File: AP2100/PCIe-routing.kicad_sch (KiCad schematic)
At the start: 40 parts

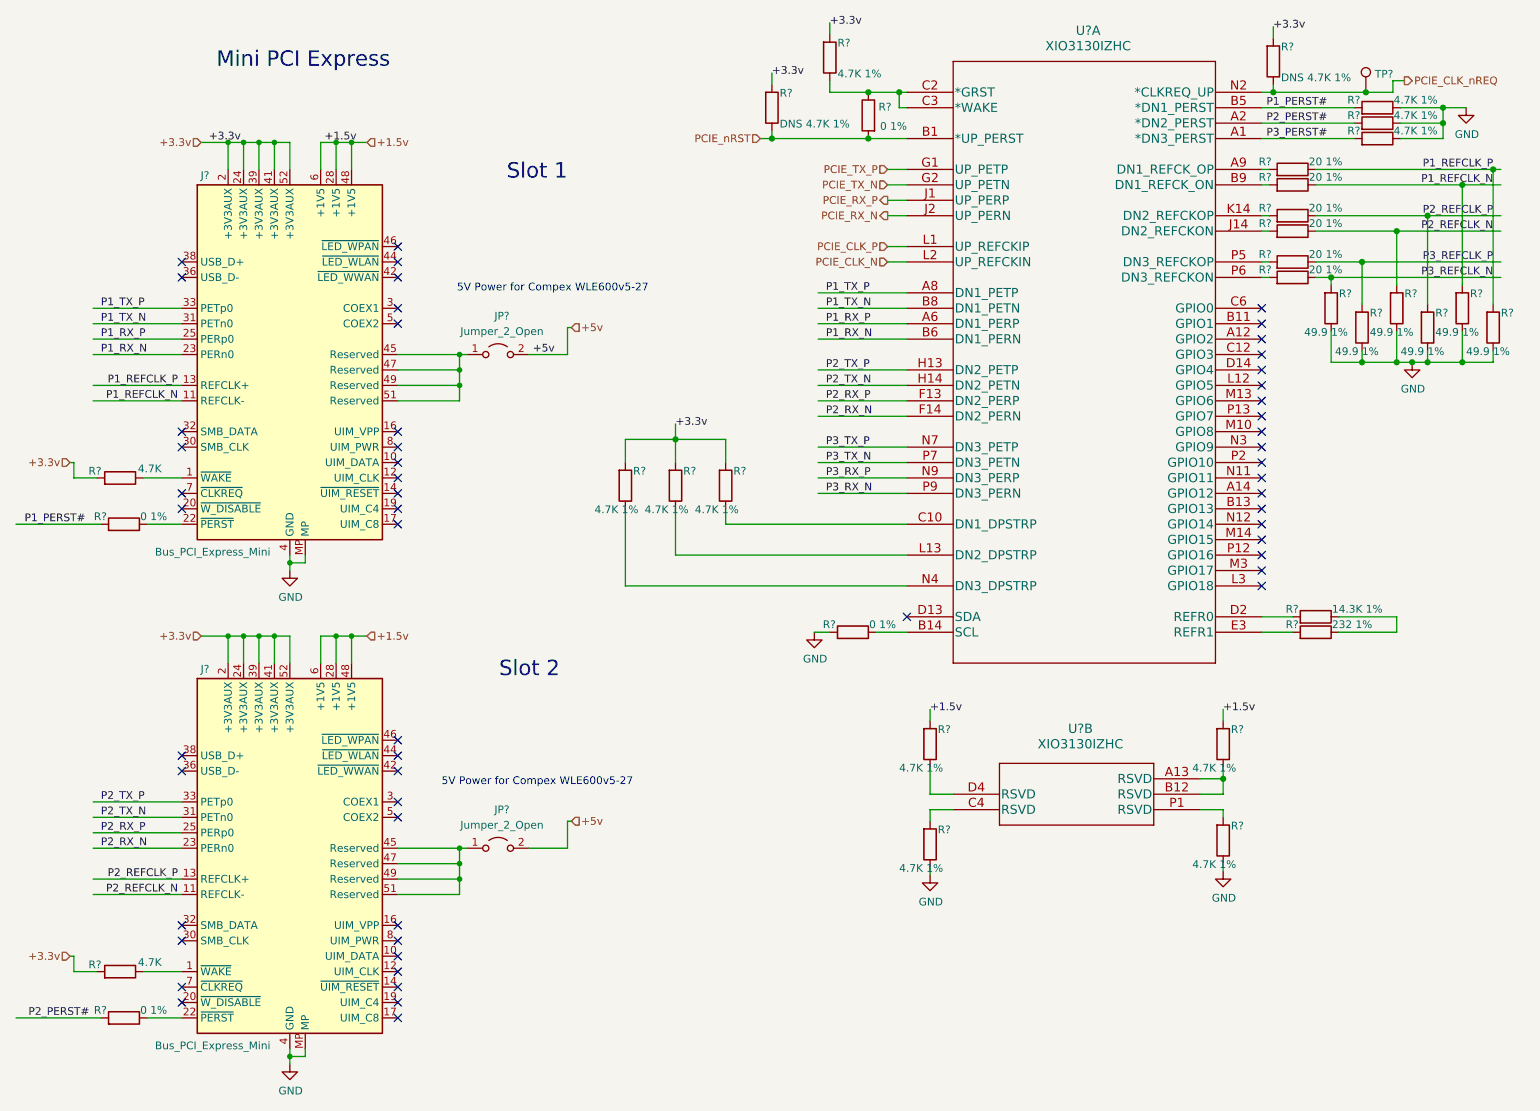
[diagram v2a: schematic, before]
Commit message: Add AP3000 single radio for security cameras. Add CM4IO Raspi board
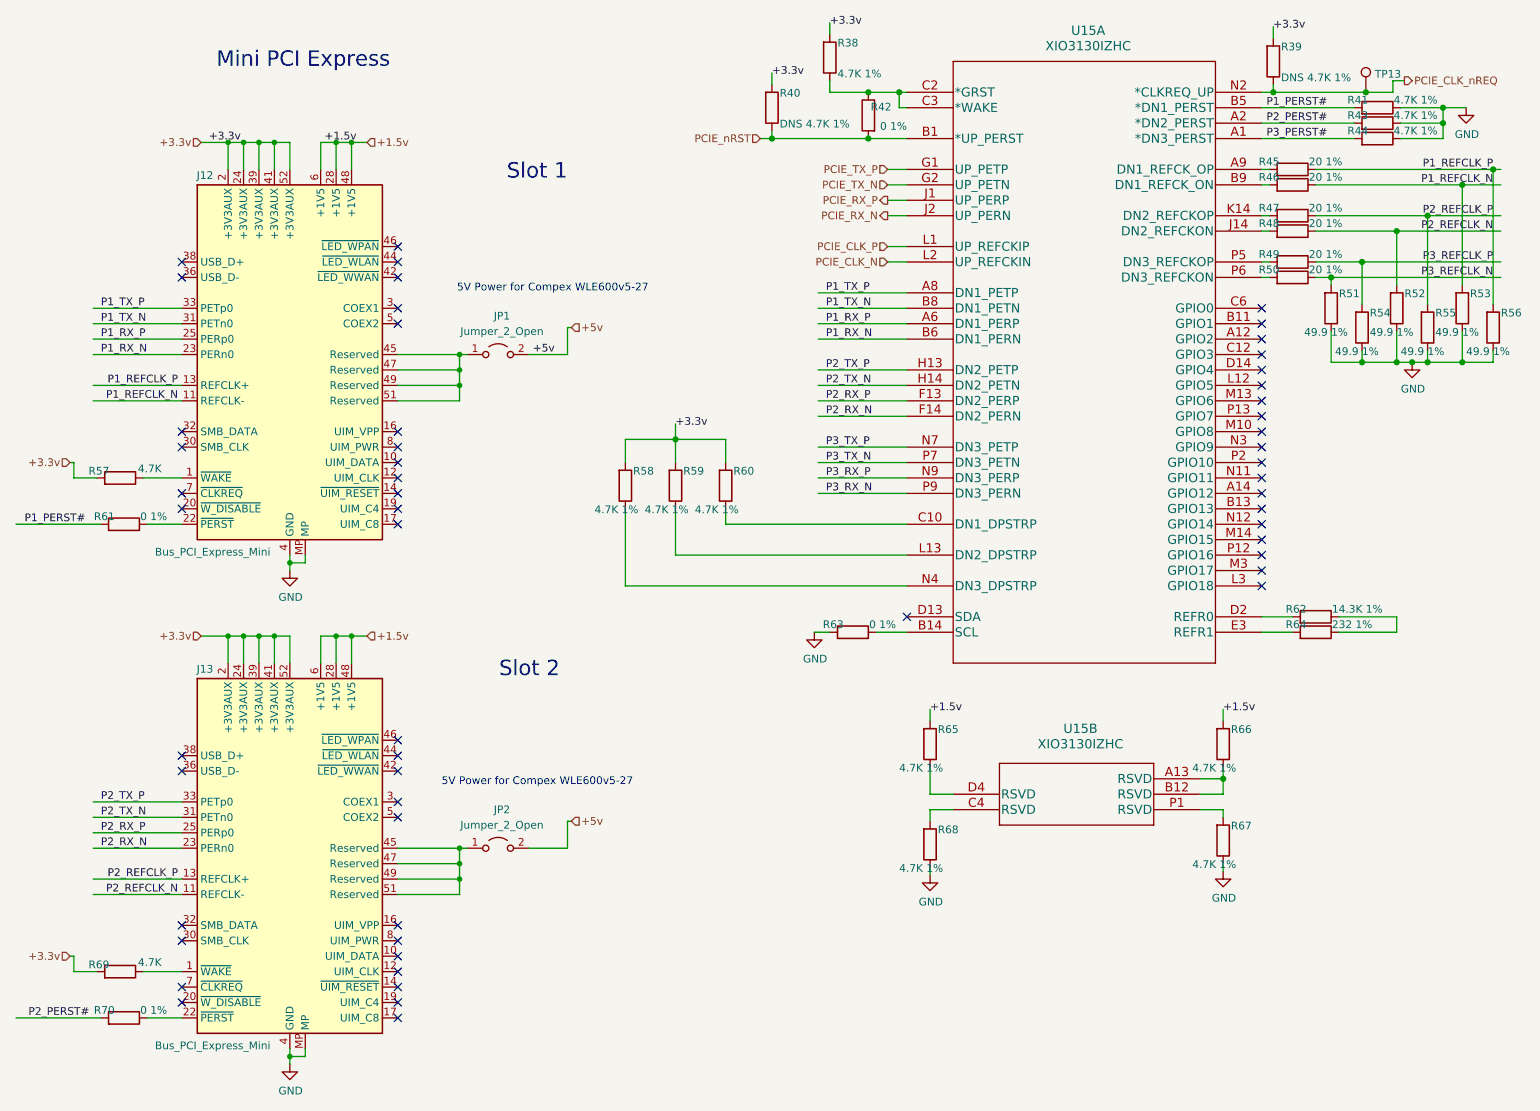
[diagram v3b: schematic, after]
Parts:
- gave numbers to parts that had none: 39
